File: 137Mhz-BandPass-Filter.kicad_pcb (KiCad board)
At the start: 2 copper layers, 13 parts

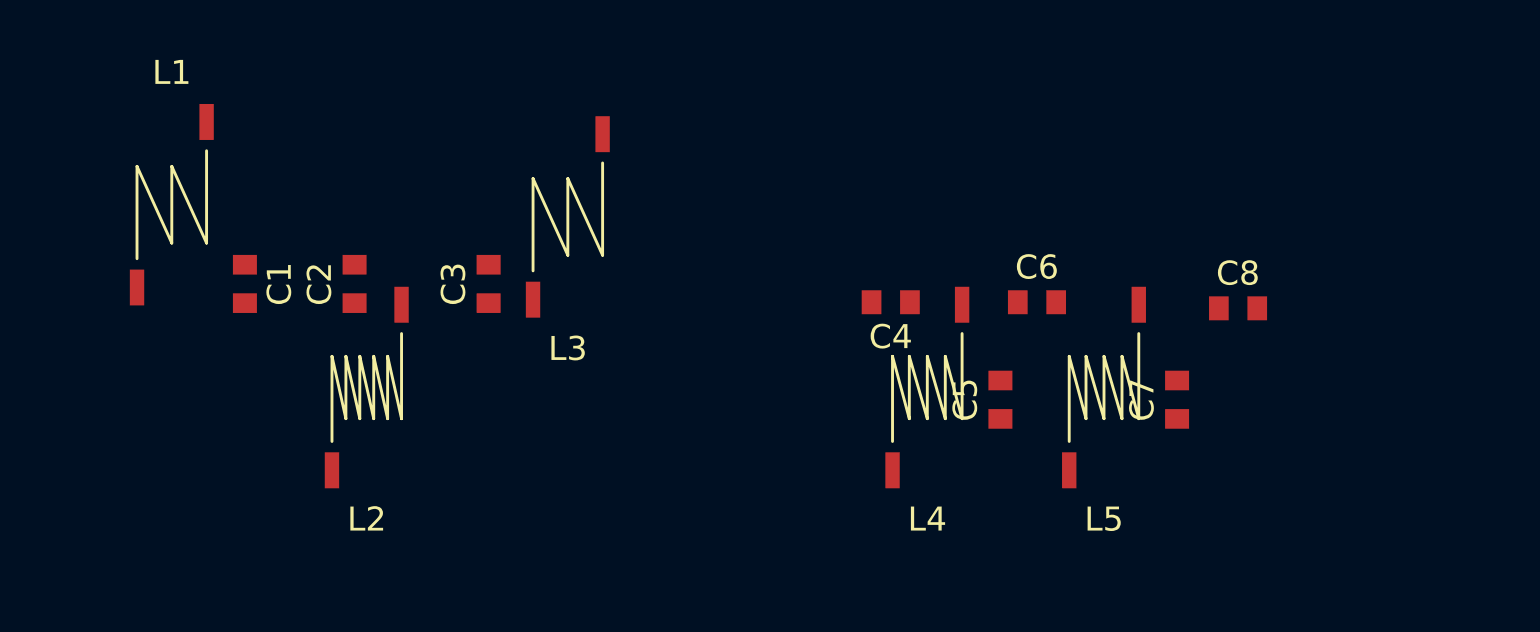
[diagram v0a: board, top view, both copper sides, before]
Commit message: Added SMA connectors, first layout try
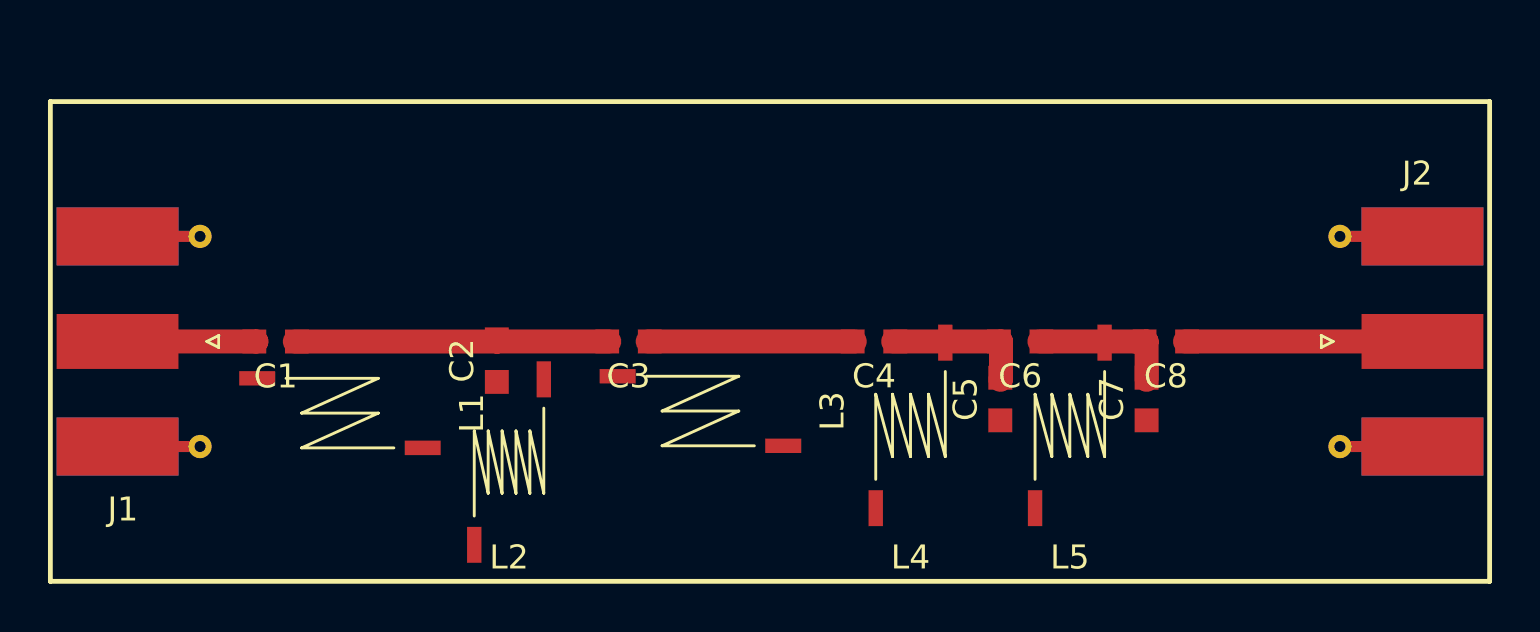
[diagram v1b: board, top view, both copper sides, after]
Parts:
- added J1: SMA, Connector_Coaxial:SMA_Molex_73251-1153_EdgeMount_Horizontal, F.Cu at (114.5, 120.0)
- added J2: SMA, Connector_Coaxial:SMA_Molex_73251-1153_EdgeMount_Horizontal, F.Cu at (165.5, 120.0)
- C1, C2, C3, C4, C5, C6, C7, C8: footprint Capacitor_SMD:C_0603_1608Metric -> Capacitor_SMD:C_0603_1608Metric_Pad0.99x1.00mm_HandSolder
- moved L1 11.2 mm to (122.1, 123.0), turned to 270 degrees
- moved L3 9.80 mm to (137.1, 122.9), turned to 270 degrees
- moved C2 6.74 mm to (128.6, 120.8)
- moved L2 6.70 mm to (129.1, 125.0)
- moved C3 6.30 mm to (134.1, 120.0), turned to 180 degrees
- moved C8 3.31 mm to (156.5, 120.0), turned to 180 degrees
- moved C1 2.72 mm to (119.4, 120.0), turned to 180 degrees
- moved L5 2.13 mm to (152.5, 123.5)
- moved C4 1.78 mm to (144.3, 120.0)
- moved C6 1.78 mm to (150.4, 120.0), turned to 180 degrees
- moved L4 1.73 mm to (145.9, 123.5)
- moved C7 1.27 mm to (155.7, 122.4)
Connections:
- C8 pad 1: (no net) -> Net-(C8-Pad1)
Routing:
- net Net-(C1-Pad1): track 0.00 -> 13.1 mm
- net Net-(C8-Pad1): track 0.00 -> 9.90 mm
- net Net-(C3-Pad1): track 0.00 -> 8.63 mm
- net Net-(C4-Pad1): track 0.00 -> 6.11 mm
- net Net-(C6-Pad1): track 0.00 -> 6.07 mm
- net Net-(C1-Pad2): track 0.00 -> 5.79 mm
- added copper zone on B.Cu, net GND
- added copper zone on F.Cu, net GND
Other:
- net class Default: clearance 0.2 -> 0.15; trace_width 0.25 -> 0.3
- rule trace_clearance: 0.2 -> 0.15

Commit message: Added 1515SQ-68N coils
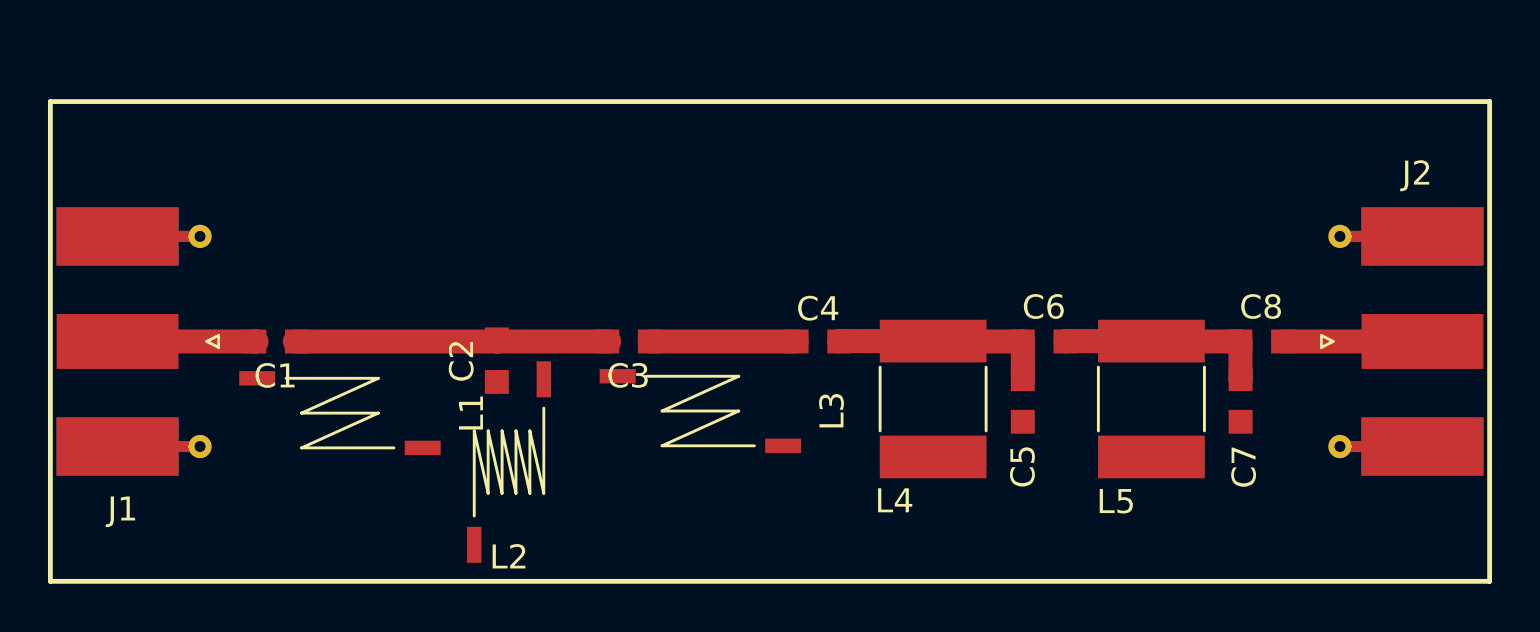
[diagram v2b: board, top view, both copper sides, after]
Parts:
- L4, L5: footprint Inductor_SMD:L_Neosid_Air-Coil_SML_4turn_HDM0431A -> kicad-footprints-master:1515SQ-68N
- moved C8 4.00 mm to (160.5, 120.0)
- moved C7 3.92 mm to (159.6, 122.5)
- moved L5 3.57 mm to (155.9, 122.4), turned to 270 degrees
- moved C4 2.33 mm to (142.0, 120.0)
- moved L4 1.45 mm to (146.8, 122.4), turned to 270 degrees
- moved C6 1.00 mm to (151.4, 120.0)
- moved C5 0.94 mm to (150.5, 122.5)
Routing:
- net Net-(C8-Pad1): track 9.90 -> 5.81 mm
- net Net-(C4-Pad1): track 6.11 -> 9.24 mm
- net Net-(C6-Pad1): track 6.07 -> 8.88 mm
- net Net-(C3-Pad1): track 8.63 -> 6.12 mm

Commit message: Notch filter removed, better inductors position
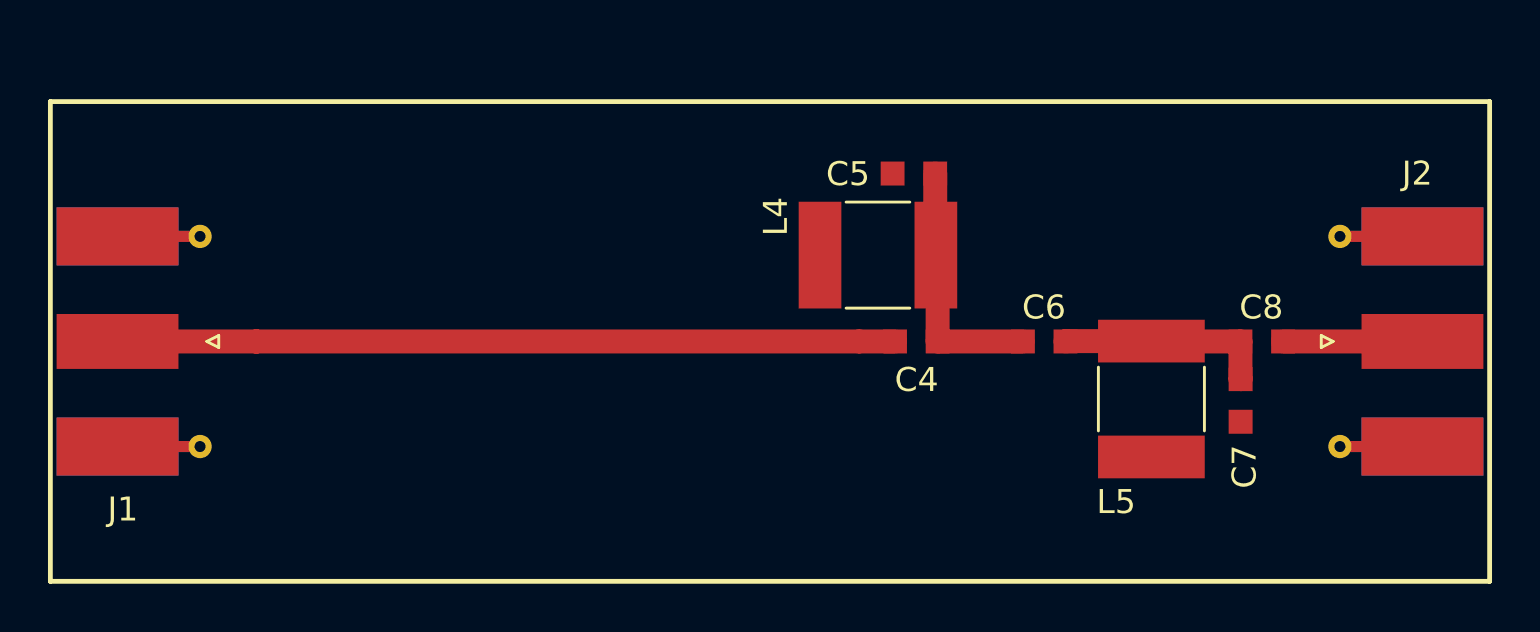
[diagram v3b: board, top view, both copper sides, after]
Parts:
- removed C1, C3: 56p, Capacitor_SMD:C_0603_1608Metric_Pad0.99x1.00mm_HandSolder
- removed C2: 22p, Capacitor_SMD:C_0603_1608Metric_Pad0.99x1.00mm_HandSolder
- removed L1, L3: 45n, Inductor_SMD:L_Neosid_Air-Coil_SML_2turn_HDM0231A
- removed L2: 126n, Inductor_SMD:L_Neosid_Air-Coil_SML_5turn_HDM0531A
- moved C5 10.5 mm to (146.0, 113.0), turned to 0 degrees
- moved L4 6.43 mm to (144.5, 116.4), turned to 180 degrees
- moved C4 4.10 mm to (146.1, 120.0)
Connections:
- C4 pad 2: Net-(C3-Pad1) -> Net-(C4-Pad2)
- J1 pad 1: Net-(C1-Pad2) -> Net-(C4-Pad2)
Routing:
- net Net-(C4-Pad2): track 0.00 -> 32.4 mm
- net Net-(C1-Pad1): track 13.1 -> 0.00 mm
- net Net-(C3-Pad1): track 6.12 -> 0.00 mm
- net Net-(C1-Pad2): track 5.79 -> 0.00 mm
- net Net-(C4-Pad1): track 9.24 -> 10.6 mm

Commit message: Coils type change, new layout, anotation reset
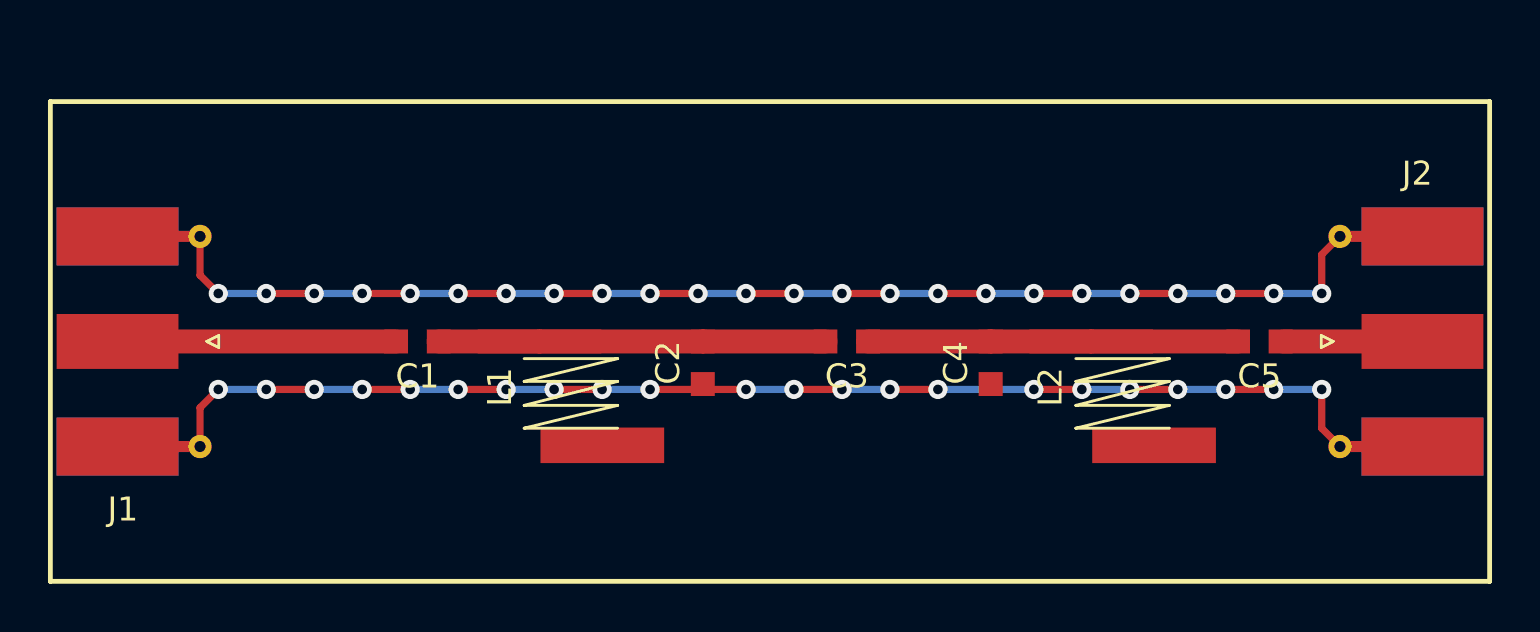
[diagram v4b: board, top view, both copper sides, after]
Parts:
- removed C6: 1p, Capacitor_SMD:C_0603_1608Metric_Pad0.99x1.00mm_HandSolder
- removed C7: 15p, Capacitor_SMD:C_0603_1608Metric_Pad0.99x1.00mm_HandSolder
- removed C8: 4p7, Capacitor_SMD:C_0603_1608Metric_Pad0.99x1.00mm_HandSolder
- removed L4, L5: 68n, kicad-footprints-master:1515SQ-68N
- added C1: 4p7, Capacitor_SMD:C_0603_1608Metric_Pad0.99x1.00mm_HandSolder, F.Cu at (125.3, 120.0)
- added C2: 15p, Capacitor_SMD:C_0603_1608Metric_Pad0.99x1.00mm_HandSolder, F.Cu at (137.2, 120.9)
- added C3: 1p, Capacitor_SMD:C_0603_1608Metric_Pad0.99x1.00mm_HandSolder, F.Cu at (143.2, 120.0)
- added L1: 68n, kicad-footprints-master:Wurth-WE-CAIR-AirCoil-4,83x3,81, F.Cu at (131.7, 122.2)
- added L2: 68n, kicad-footprints-master:Wurth-WE-CAIR-AirCoil-4,83x3,81, F.Cu at (154.7, 122.2)
- C4: value 4p7 -> 15p
- C5: value 15p -> 4p7
- moved C5 16.0 mm to (160.4, 120.0), turned to 180 degrees
- moved C4 3.22 mm to (149.2, 120.9), turned to 90 degrees
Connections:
- C4 pad 1: Net-(C4-Pad1) -> GND
- C4 pad 2: Net-(C4-Pad2) -> Net-(C3-Pad1)
- C5 pad 1: GND -> Net-(C5-Pad1)
- C5 pad 2: Net-(C4-Pad1) -> Net-(C3-Pad1)
- J1 pad 1: Net-(C4-Pad2) -> Net-(C1-Pad2)
- J2 pad 1: Net-(C8-Pad1) -> Net-(C5-Pad1)
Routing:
- net GND: track 0.00 -> 102.8 mm, vias 0 -> 46
- net Net-(C4-Pad2): track 32.4 -> 0.00 mm
- net Net-(C1-Pad1): track 0.00 -> 16.1 mm
- net Net-(C3-Pad1): track 0.00 -> 15.4 mm
- net Net-(C1-Pad2): track 0.00 -> 11.6 mm
- net Net-(C4-Pad1): track 10.6 -> 0.00 mm
- net Net-(C6-Pad1): track 8.88 -> 0.00 mm
- net Net-(C8-Pad1): track 5.81 -> 0.00 mm
- net Net-(C5-Pad1): track 0.00 -> 5.81 mm
